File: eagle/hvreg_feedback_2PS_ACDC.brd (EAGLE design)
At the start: 128.5 x 101.9 mm, 14 parts

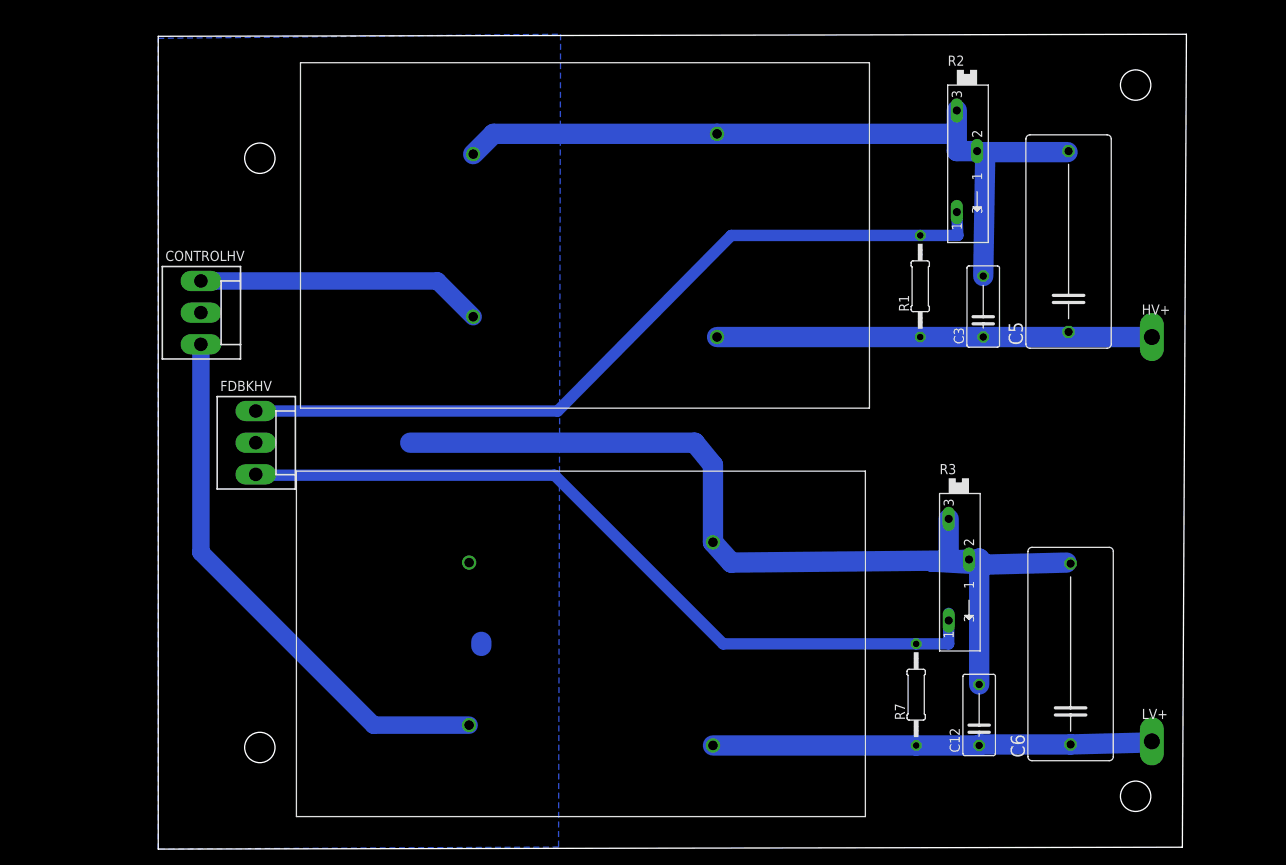
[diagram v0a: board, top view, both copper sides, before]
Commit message: capacitor bank
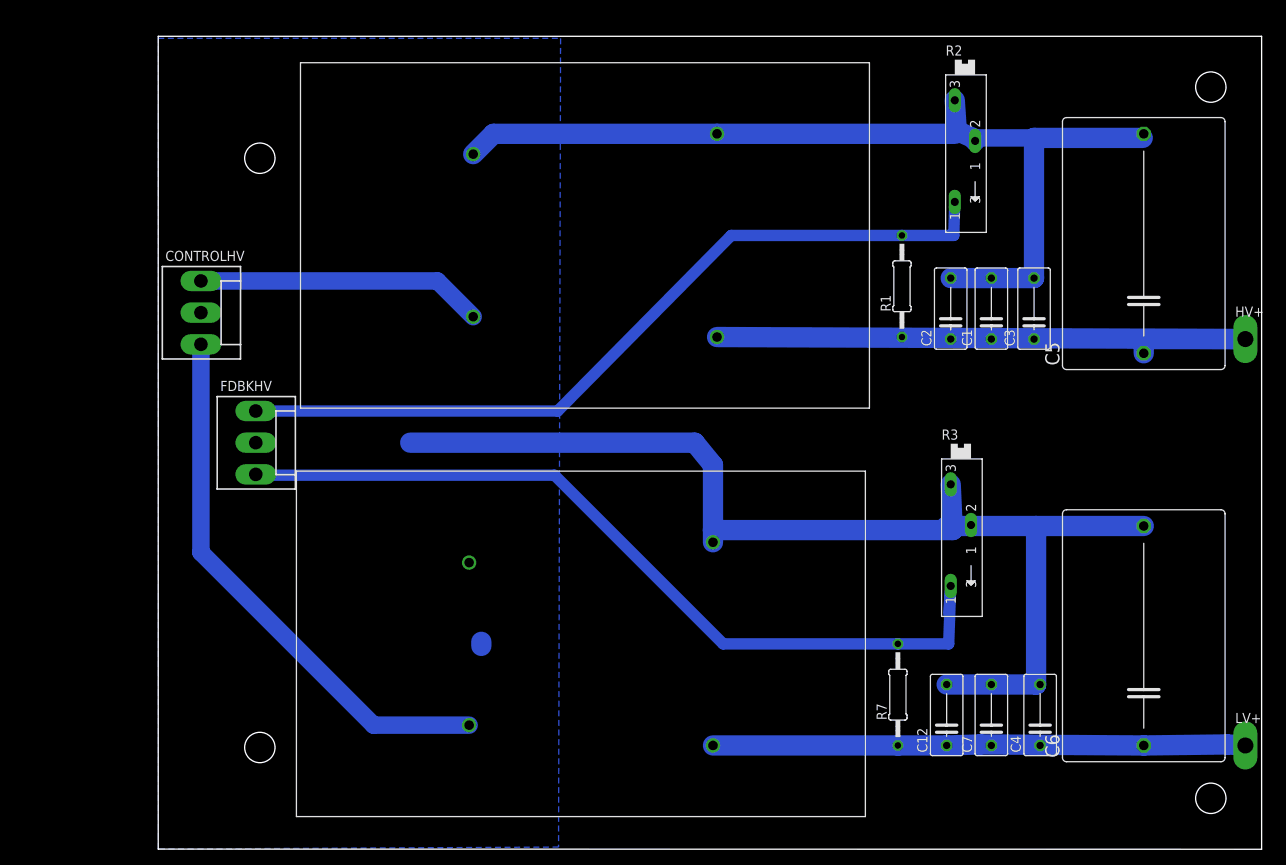
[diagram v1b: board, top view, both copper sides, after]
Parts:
- added C1, C4: 1n, rcl:C075-042X103
- added C2, C7: 10p, rcl:C075-042X103
- C5, C6: device rcl:C225-108X268 -> rcl:C275-205X316
- moved LV+ 11.7 mm to (153.7, 12.7)
- moved HV+ 11.7 mm to (153.7, 63.5)
- moved C6 9.43 mm to (141.0, 26.4)
- moved C5 9.40 mm to (141.0, 75.4)
- moved C3 6.36 mm to (127.3, 67.3)
- moved R3 4.33 mm to (118.1, 38.4)
- moved C12 4.06 mm to (116.3, 16.5)
- moved R1 2.29 mm to (110.7, 70.1)
- moved R7 2.29 mm to (110.2, 19.1)
- moved R2 1.30 mm to (118.6, 86.4)
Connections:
- net GND: now also C1.2, C2.2, C4.2, C7.2
- net N$1: now also C1.1, C2.1
- net N$2: now also C4.1, C7.1
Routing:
- net GND: track 222.6 -> 258.4 mm
- net N$1: track 54.4 -> 80.5 mm
- net N$2: track 55.0 -> 66.6 mm
- net N$8: track 99.5 -> 106.3 mm
- net N$3: track 99.8 -> 100.6 mm
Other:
- board size 128.5 x 101.9 mm -> 137.9 x 101.6 mm

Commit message: IXYS board solution, gatedriver components
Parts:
- added D1, D2: 1N4004, diode:DO41-10
- moved R3 24.1 mm to (95.2, 46.0)
- moved HV+ 21.3 mm to (133.6, 56.4), turned to 90 degrees
- moved LV+ 19.8 mm to (133.9, 13.2), turned to 90 degrees
- moved C6 19.3 mm to (123.2, 34.0)
- moved C7 19.3 mm to (104.1, 24.1)
- moved R7 19.3 mm to (92.5, 26.7)
- moved C12 19.3 mm to (98.6, 24.1)
- moved C4 19.3 mm to (110.2, 24.1)
- moved C5 17.9 mm to (123.2, 77.7)
- moved C1 17.8 mm to (104.1, 67.8)
- moved C2 17.8 mm to (99.1, 67.8)
- moved C3 17.8 mm to (109.5, 67.8)
- moved CONTROLHV 17.8 mm to (5.33, 67.3)
- moved R1 17.8 mm to (93.0, 70.6)
- moved R2 17.5 mm to (101.3, 89.4)
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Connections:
- new net N$6: D1.C, HV+.TP
- new net N$7: D2.C, LV+.TP
- net N$1: now also D1.A; no longer HV+.TP
- net N$2: now also D2.A; no longer LV+.TP
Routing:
- net N$1: track 80.5 -> 61.0 mm
- net N$8: track 106.3 -> 95.1 mm
- net N$7: track 0.00 -> 10.8 mm
- net N$6: track 0.00 -> 10.2 mm
- net GND: track 258.4 -> 267.2 mm
- net N$3: track 100.6 -> 103.1 mm
- net N$2: track 66.6 -> 64.5 mm
- net N$5: track 68.5 -> 70.0 mm
- net N$4: track 35.9 -> 37.2 mm
